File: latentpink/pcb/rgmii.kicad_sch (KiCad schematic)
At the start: 63 parts, among them J5 0826-1G1T-23-F, U2 XC7K160T-2FBG484C, U21 ECX2-LMV-3CN-125.000-TR, U22 ECS-2016MVQ-250-CN, U64 RCLAMP0514M, U65 RCLAMP0514M, U9 KSZ9031RN

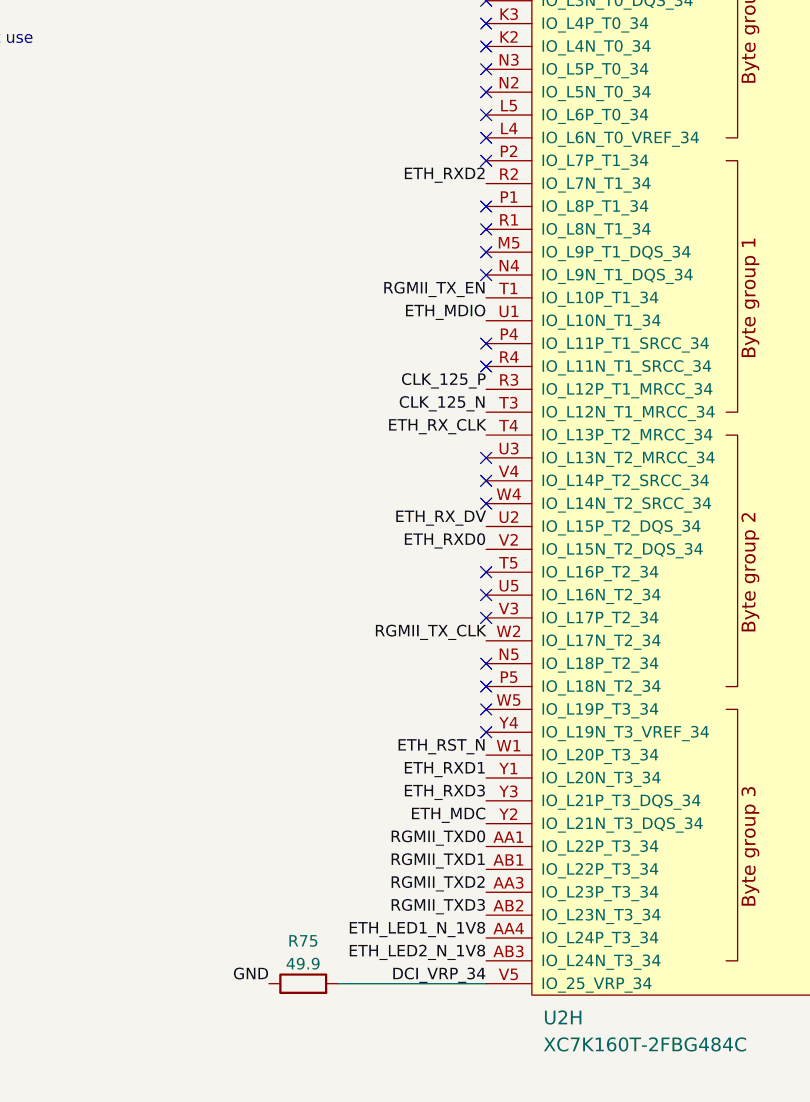
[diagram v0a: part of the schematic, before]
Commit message: Routing of northwest corner
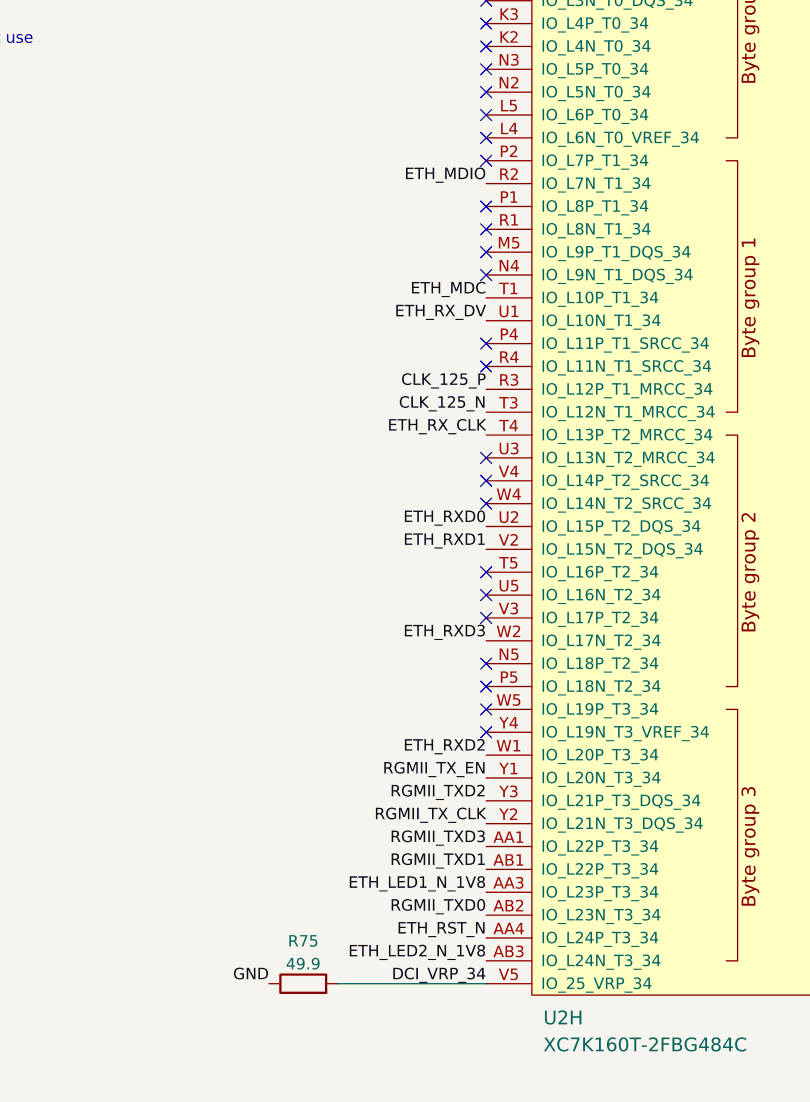
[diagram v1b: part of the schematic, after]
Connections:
- net ETH_LED1_N_1V8: now also U2.AA3 (IO_L23P_T3_34); no longer U2.AA4 (IO_L24P_T3_34)
- net ETH_MDC: now also U2.T1 (IO_L10P_T1_34); no longer U2.Y2 (IO_L21N_T3_DQS_34)
- net ETH_MDIO: now also U2.R2 (IO_L7N_T1_34); no longer U2.U1 (IO_L10N_T1_34)
- net ETH_RST_N: now also U2.AA4 (IO_L24P_T3_34); no longer U2.W1 (IO_L20P_T3_34)
- net ETH_RXD0: now also U2.U2 (IO_L15P_T2_DQS_34); no longer U2.V2 (IO_L15N_T2_DQS_34)
- net ETH_RXD1: now also U2.V2 (IO_L15N_T2_DQS_34); no longer U2.Y1 (IO_L20N_T3_34)
- net ETH_RXD2: now also U2.W1 (IO_L20P_T3_34); no longer U2.R2 (IO_L7N_T1_34)
- net ETH_RXD3: now also U2.W2 (IO_L17N_T2_34); no longer U2.Y3 (IO_L21P_T3_DQS_34)
- net ETH_RX_DV: now also U2.U1 (IO_L10N_T1_34); no longer U2.U2 (IO_L15P_T2_DQS_34)
- net RGMII_TXD0: now also U2.AB2 (IO_L23N_T3_34); no longer U2.AA1 (IO_L22P_T3_34)
- net RGMII_TXD2: now also U2.Y3 (IO_L21P_T3_DQS_34); no longer U2.AA3 (IO_L23P_T3_34)
- net RGMII_TXD3: now also U2.AA1 (IO_L22P_T3_34); no longer U2.AB2 (IO_L23N_T3_34)
- net RGMII_TX_CLK: now also U2.Y2 (IO_L21N_T3_DQS_34); no longer U2.W2 (IO_L17N_T2_34)
- net RGMII_TX_EN: now also U2.Y1 (IO_L20N_T3_34); no longer U2.T1 (IO_L10P_T1_34)
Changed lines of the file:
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@@
     (effects (font (size 1.27 1.27)) (justify right bottom))
   )
-  (label "ETH_RXD3" (at 293.37 143.51 180)
-    (effects (font (size 1.27 1.27)) (justify right bottom))
-  )
-  (label "RGMII_TX_CLK" (at 293.37 125.73 180)
+  (label "ETH_RXD3" (at 293.37 125.73 180)
+    (effects (font (size 1.27 1.27)) (justify right bottom))
+  )
+  (label "RGMII_TX_CLK" (at 293.37 146.05 180)
     (effects (font (size 1.27 1.27)) (justify right bottom))
   )
@@
     (effects (font (size 1.27 1.27)) (justify right bottom))
   )
-  (label "ETH_LED1_N_1V8" (at 293.37 158.75 180)
-    (effects (font (size 1.27 1.27)) (justify right bottom))
-  )
-  (label "ETH_RXD2" (at 293.37 74.93 180)
+  (label "ETH_LED1_N_1V8" (at 293.37 153.67 180)
+    (effects (font (size 1.27 1.27)) (justify right bottom))
+  )
+  (label "ETH_RXD2" (at 293.37 138.43 180)
     (effects (font (size 1.27 1.27)) (justify right bottom))
   )
@@
     (effects (font (size 1.27 1.27)) (justify left bottom))
   )
-  (label "RGMII_TXD3" (at 293.37 156.21 180)
+  (label "RGMII_TXD3" (at 293.37 148.59 180)
     (effects (font (size 1.27 1.27)) (justify right bottom))
   )
@@
     (effects (font (size 1.27 1.27)) (justify left bottom))
   )
-  (label "ETH_RXD1" (at 293.37 140.97 180)
+  (label "ETH_RXD1" (at 293.37 115.57 180)
     (effects (font (size 1.27 1.27)) (justify right bottom))
   )
@@
     (effects (font (size 1.27 1.27)) (justify right bottom))
   )
-  (label "RGMII_TX_EN" (at 293.37 87.63 180)
+  (label "RGMII_TX_EN" (at 293.37 140.97 180)
     (effects (font (size 1.27 1.27)) (justify right bottom))
   )
@@
     (effects (font (size 1.27 1.27)) (justify right bottom))
   )
-  (label "RGMII_TXD0" (at 293.37 148.59 180)
+  (label "RGMII_TXD0" (at 293.37 156.21 180)
     (effects (font (size 1.27 1.27)) (justify right bottom))
   )
@@
     (effects (font (size 1.27 1.27)) (justify right bottom))
   )
-  (label "ETH_MDC" (at 293.37 146.05 180)
+  (label "ETH_MDC" (at 293.37 87.63 180)
     (effects (font (size 1.27 1.27)) (justify right bottom))
   )
@@
     (effects (font (size 1.27 1.27)) (justify right bottom))
   )
-  (label "ETH_MDIO" (at 293.37 90.17 180)
+  (label "ETH_MDIO" (at 293.37 74.93 180)
     (effects (font (size 1.27 1.27)) (justify right bottom))
   )
@@
     (effects (font (size 1.27 1.27)) (justify right bottom))
   )
-  (label "ETH_RST_N" (at 293.37 138.43 180)
+  (label "ETH_RST_N" (at 293.37 158.75 180)
     (effects (font (size 1.27 1.27)) (justify right bottom))
   )
@@
     (effects (font (size 1.27 1.27)) (justify right bottom))
   )
-  (label "RGMII_TXD2" (at 293.37 153.67 180)
+  (label "RGMII_TXD2" (at 293.37 143.51 180)
     (effects (font (size 1.27 1.27)) (justify right bottom))
   )
@@
     (effects (font (size 1.27 1.27)) (justify left bottom))
   )
-  (label "ETH_RX_DV" (at 293.37 113.03 180)
+  (label "ETH_RX_DV" (at 293.37 90.17 180)
     (effects (font (size 1.27 1.27)) (justify right bottom))
   )
@@
     (effects (font (size 1.27 1.27)) (justify right bottom))
   )
-  (label "ETH_RXD0" (at 293.37 115.57 180)
-    (effects (font (size 1.27 1.27)) (justify right bottom))
-  )
+  (label "ETH_RXD0" (at 293.37 113.03 180)
+    (effects (font (size 1.27 1.27)) (justify right bottom))
+  )

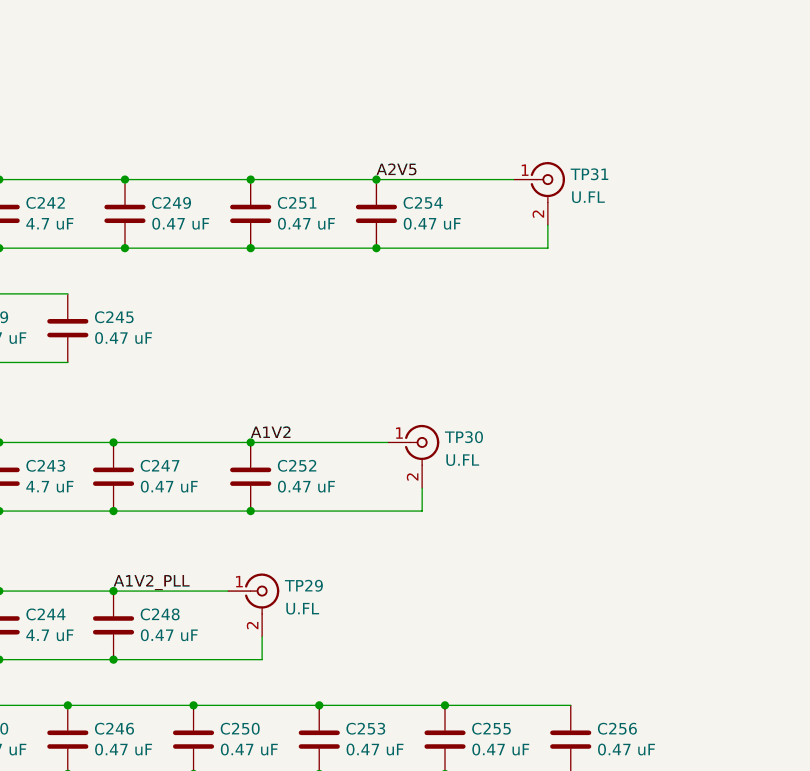
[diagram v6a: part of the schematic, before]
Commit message: Updated schematic with notes on power rail sequencing bug found during bringup
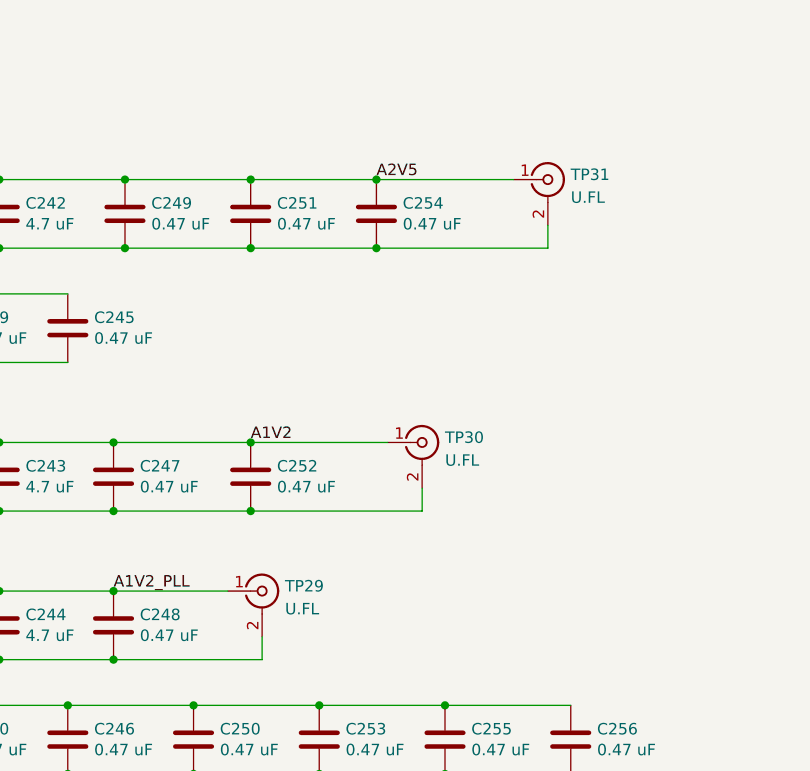
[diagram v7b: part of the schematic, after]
